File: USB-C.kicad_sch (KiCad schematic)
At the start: 4 parts, among them J3 USB-C Connectors

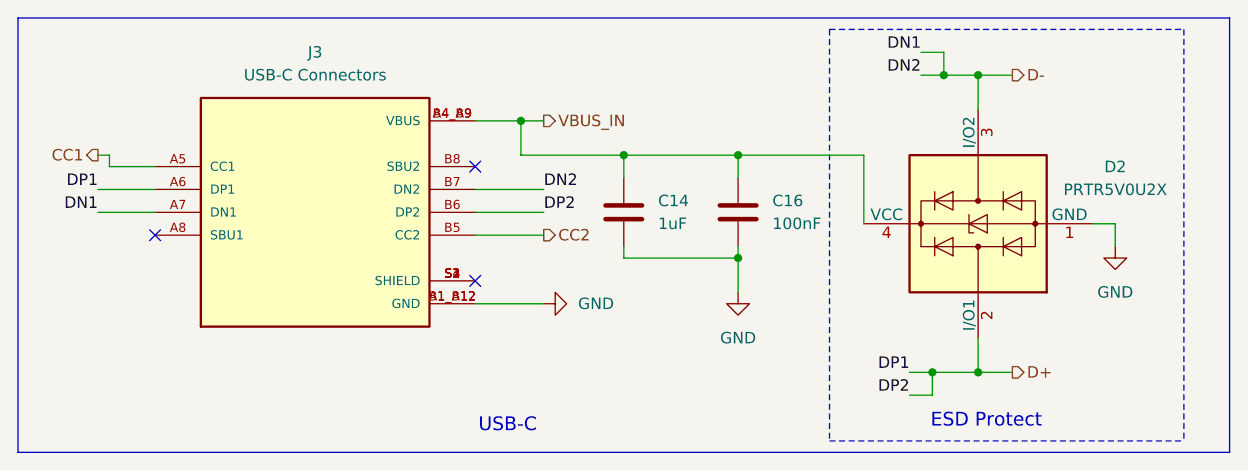
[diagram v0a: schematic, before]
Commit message: Feat: 개발보드 버전으로 PCB 변경
수정사항

단가 감소
- PCB Board size up (50x50)
- blind via 제거 (전체 레이아웃 수정)
- AVDD 전력평면 추가
- ADS1299 안쓰는핀 GND
- ADS1299 배치 변경 (Layout Reference 적용)

개발보드만 적용사항
- Pin Header size up 1.27 → 2.54mm
- PCB Size 50x50(mm)
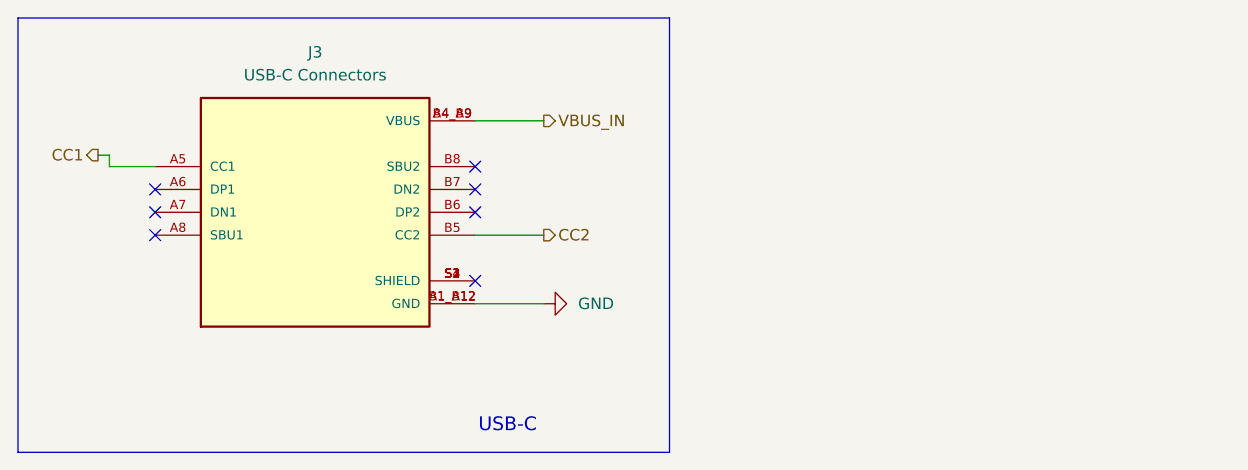
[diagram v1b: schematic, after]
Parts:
- removed C14: 1uF, Capacitor_SMD:C_0402_1005Metric, symbol Device:C
- removed C16: 100nF, Capacitor_SMD:C_0402_1005Metric, symbol Device:C
- removed D2: PRTR5V0U2X, Package_TO_SOT_SMD:SOT-143, symbol Power_Protection:PRTR5V0U2X
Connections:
- net D+: no longer names the net of J3.A6 (DP1)
- net D+: no longer J3.B6 (DP2)
- net D-: no longer names the net of J3.A7 (DN1)
- net D-: no longer J3.B7 (DN2)
- no-connect marks 3 -> 7
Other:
- note removed: "ESD Protect"
